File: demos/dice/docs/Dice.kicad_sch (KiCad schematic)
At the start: 23 parts, among them U2 CD4017

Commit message: export: kicad_sch — Phase 2.5b: layered placement, wire routing, KiCad 10 compatibility (#23)
* export: kicad_sch — Phase 2.5b: layered placement + routing + KiCad 9 fix

Placement (placement.py, complete rewrite):
- Replaces naive grid with Layered Signal Flow algorithm (spec §5 stages 1–8)
- Stage 1: band classification — power chips/rails at top, LEDs at bottom,
  everything else in the signal band
- Stage 2: signal-flow DAG via BFS from Rail/Connector sources; layer = BFS
  distance from nearest source
- Stage 3–4: place within (band, layer) cells at 1500-mil (38.1 mm) same-band
  spacing, 1000-mil inter-band gutter, 25.4 mm page margin
- Stage 6: cluster breakup — up to 10 iterations shifting same-band parts
  that land closer than 0.9× SAME_BAND_SPACING_MM
- Stage 8: page sized to fit (A4 → A3 → A2 → A1)
- grid_place() and sheet_size_mm() kept as shims for backward-compat

Routing (routing.py, new file):
- route_net(): connects stub ends with Manhattan L-shapes (horizontal first)
- find_junctions(): returns points where ≥3 wire endpoints coincide
- renderer uses routed wires between signal-net stub ends

Hierarchical (hierarchical.py, new file):
- collect_boards(), is_multi_board(), sub_sheet_filename() — interface stub
  for multi-Board sub-sheet emission (full implementation deferred)

KiCad 9 sub-symbol name fix (library_loader.py):
- KiCad 9 schematics expect sub-symbols nested inside their parent in
  lib_symbols to use the bare name (R_0_1, LED_0_1, 4069_1_0) — NOT the
  lib-qualified name (Device:R_0_1, Device:LED_0_1, 4xxx:4069_1_0)
- Fixed _qualify_names() to add the lib: prefix only to the exact parent
  symbol name using a lookahead (?=") that prevents sub-unit names from
  being qualified

Tests (+25 tests):
- test_placement.py: band classification, all-on-grid, determinism,
  minimum spacing, power < signal < indicator Y ordering, page sizing
- test_routing.py: H/V segments, L-shapes, orthogonality, grid snap,
  junction detection

Golden files re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
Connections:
- net Net-(D10-anode) is gone; now on net Net-(D1-cathode): D10.1 (K), D11.1 (K), R3.1, R3.2
- net Net-(D12-anode) is gone; now on net Net-(D1-cathode): D12.1 (K), D13.1 (K), R4.1, R4.2
- net Net-(D8-anode) is gone; now on net Net-(D1-cathode): D8.1 (K), D9.1 (K), R2.1, R2.2
- net Net-(D1-cathode): now also R5.1, R5.2, R6.1, R6.2, R7.1, R7.2
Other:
- moved on the sheet: C1, C2, D1, D10, D11, D12, D13, D2, D3, D4, D5, D6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

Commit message: framework: passive + diode terminals mandatory (#30)
Continuation of the LED.cathode regression fix (#29). Resistor,
Capacitor, Inductor, and every Diode subclass had their terminals
declared `mandatory=False` with the same "structurally inert under
graph evaluation" justification — letting demos declare BOM-only
timing / decoupling / pull-up parts without wiring them, then ship
breadboard SVGs and netlists where those parts sat orphaned.

A real resistor / capacitor / inductor / diode with a dangling
terminal does nothing. Marking the ports mandatory closes the
silent regression at the framework layer.

  - `src/components/passives/{resistor,capacitor,inductor}.py` and
    every diode subclass under `src/components/diodes/` now declare
    their terminals `mandatory=True`.
  - `tests/components/test_{resistor,capacitor,inductor}.py`:
    regression tests pin the new contract per component.
  - `tests/components/test_diode_mandatory_terminals.py` (new):
    parametrized over D1N4001 / D1N4007 / D1N4148 / D1N4728A /
    D1N4733A / D1N4742A / D1N5817.
  - Six demos (`backup_power`, `bldc_motor`, `dice`,
    `doorbell_protector`, `fan_cooling`, `isolated_rs232`) had
    declared-but-unwired passives — each now wires them either to
    their datasheet-correct net (e.g. DoorbellProtector's flyback
    diode anode joins the relay coil_minus net) or as an isolated
    0-Ω passthrough with `dynamically_driven=True` where the part
    is genuinely BOM-only and the voltage-only simulator can't
    honour its behaviour. Comments at each call site explain
    which kind.
  - Test fixtures across CLI, refdes, format-roundtrip, kicad
    import, and per-format renderer tests updated so they still
    pin down the specific error each one exists to catch without
    tripping the new mandatory-pin check first.
  - All demo docs regenerated; goldens refreshed.

After this commit the breadboard SVGs show every BOM part connected
to something — no more orphaned caps and resistors float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
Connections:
- net Net-(D1-cathode) is gone; now on net VCC: D10.1 (K), D11.1 (K), D12.1 (K), D13.1 (K), D7.1 (K), D8.1 (K), D9.1 (K), R1.1, R1.2, R2.1, R2.2, R3.1, R3.2, R4.1, R4.2, R5.1, R5.2, R6.1, R6.2, R7.1, R7.2
- net VCC: now reaches C2.1
- net VCC: now also C1.1, C1.2, C2.2
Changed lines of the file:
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@@
     (stroke (width 0) (type default))
+  )
+  (symbol
+    (lib_id "power:VCC")
+    (at 63.5 641.35 90)
+    (unit 1)
+    (exclude_from_sim no)
+    (in_bom yes)
+    (on_board yes)
+    (dnp no)
+    (property "Reference" "#PWR"
+      (at 63.5 641.35 0)
+      (effects (font (size 1.27 1.27)) (hide yes))
+    )
+    (property "Value" "VCC"
+      (at 63.5 641.35 0)
+      (effects (font (size 1.27 1.27)))
+    )
+    (pin "1")
   )
   (wire
     (pts (xy 63.5 631.19) (xy 63.5 628.65))
     (stroke (width 0) (type default))
+  )
+  (symbol
+    (lib_id "power:VCC")
+    (at 63.5 628.65 90)
+    (unit 1)
+    (exclude_from_sim no)
+    (in_bom yes)
+    (on_board yes)
+    (dnp no)
+    (property "Reference" "#PWR"
+      (at 63.5 628.65 0)
+      (effects (font (size 1.27 1.27)) (hide yes))
+    )
+    (property "Value" "VCC"
+      (at 63.5 628.65 0)
+      (effects (font (size 1.27 1.27)))
+    )
+    (pin "1")
   )
   (symbol
@@
     (stroke (width 0) (type default))
   )
+  (symbol
+    (lib_id "power:VCC")
+    (at 63.5 679.45 90)
+    (unit 1)
+    (exclude_from_sim no)
+    (in_bom yes)
+    (on_board yes)
+    (dnp no)
+    (property "Reference" "#PWR"
+      (at 63.5 679.45 0)
+      (effects (font (size 1.27 1.27)) (hide yes))
+    )
+    (property "Value" "VCC"
+      (at 63.5 679.45 0)
+      (effects (font (size 1.27 1.27)))
+    )
+    (pin "1")
+  )
   (wire
     (pts (xy 63.5 669.29) (xy 63.5 666.75))
     (stroke (width 0) (type default))
+  )
+  (symbol
+    (lib_id "power:VCC")
+    (at 63.5 666.75 90)
+    (unit 1)
+    (exclude_from_sim no)
+    (in_bom yes)
+    (on_board yes)
+    (dnp no)
+    (property "Reference" "#PWR"
+      (at 63.5 666.75 0)
+      (effects (font (size 1.27 1.27)) (hide yes))
+    )
+    (property "Value" "VCC"
+      (at 63.5 666.75 0)
+      (effects (font (size 1.27 1.27)))
+    )
+    (pin "1")
   )
   (symbol
@@
     (stroke (width 0) (type default))
   )
+  (symbol
+    (lib_id "power:VCC")
+    (at 63.5 717.55 90)
+    (unit 1)
+    (exclude_from_sim no)
+    (in_bom yes)
+    (on_board yes)
+    (dnp no)
+    (property "Reference" "#PWR"
+      (at 63.5 717.55 0)
+      (effects (font (size 1.27 1.27)) (hide yes))
+    )
+    (property "Value" "VCC"
+      (at 63.5 717.55 0)
+      (effects (font (size 1.27 1.27)))
+    )
+    (pin "1")
+  )
   (wire
     (pts (xy 63.5 707.39) (xy 63.5 704.85))
     (stroke (width 0) (type default))
+  )
+  (symbol
+    (lib_id "power:VCC")
+    (at 63.5 704.85 90)
+    (unit 1)
+    (exclude_from_sim no)
+    (in_bom yes)
+    (on_board yes)
+    (dnp no)
+    (property "Reference" "#PWR"
+      (at 63.5 704.85 0)
+      (effects (font (size 1.27 1.27)) (hide yes))
+    )
+    (property "Value" "VCC"
+      (at 63.5 704.85 0)
+      (effects (font (size 1.27 1.27)))
+    )
+    (pin "1")
   )
   (symbol
@@
     (stroke (width 0) (type default))
   )
+  (symbol
+    (lib_id "power:VCC")
+    (at 63.5 31.75 90)
+    (unit 1)
+    (exclude_from_sim no)
+    (in_bom yes)
+    (on_board yes)
+    (dnp no)
+    (property "Reference" "#PWR"
+      (at 63.5 31.75 0)
+      (effects (font (size 1.27 1.27)) (hide yes))
+    )
+    (property "Value" "VCC"
+      (at 63.5 31.75 0)
+      (effects (font (size 1.27 1.27)))
+    )
+    (pin "1")
+  )
   (wire
     (pts (xy 63.5 21.59) (xy 63.5 19.05))
     (stroke (width 0) (type default))
+  )
+  (symbol
+    (lib_id "power:VCC")
+    (at 63.5 19.05 90)
+    (unit 1)
+    (exclude_from_sim no)
+    (in_bom yes)
+    (on_board yes)
+    (dnp no)
+    (property "Reference" "#PWR"
+      (at 63.5 19.05 0)
+      (effects (font (size 1.27 1.27)) (hide yes))
+    )
+    (property "Value" "VCC"
+      (at 63.5 19.05 0)
+      (effects (font (size 1.27 1.27)))
+    )
+    (pin "1")
   )
   (symbol
@@
     (stroke (width 0) (type default))
   )
+  (symbol
+    (lib_id "power:VCC")
+    (at 63.5 69.85 90)
+    (unit 1)
+    (exclude_from_sim no)
+    (in_bom yes)
+    (on_board yes)
+    (dnp no)
+    (property "Reference" "#PWR"
+      (at 63.5 69.85 0)
+      (effects (font (size 1.27 1.27)) (hide yes))
+    )
+    (property "Value" "VCC"
+      (at 63.5 69.85 0)
+      (effects (font (size 1.27 1.27)))
+    )
+    (pin "1")
+  )
   (wire
     (pts (xy 63.5 59.69) (xy 63.5 57.15))
@@
   )
   (symbol
+    (lib_id "power:VCC")
+    (at 63.5 57.15 90)
+    (unit 1)
+    (exclude_from_sim no)
+    (in_bom yes)
+    (on_board yes)
+    (dnp no)
+    (property "Reference" "#PWR"
+      (at 63.5 57.15 0)
+      (effects (font (size 1.27 1.27)) (hide yes))
+    )
+    (property "Value" "VCC"
+      (at 63.5 57.15 0)
+      (effects (font (size 1.27 1.27)))
+    )
+    (pin "1")
+  )
+  (symbol

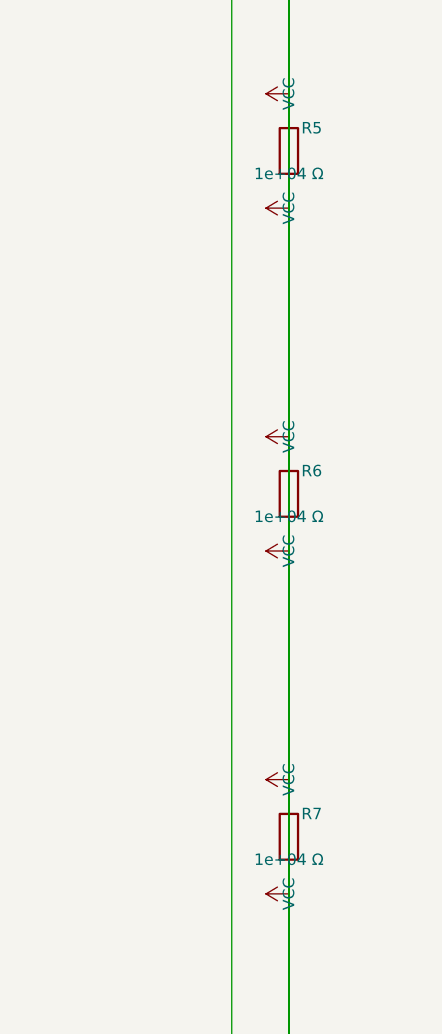
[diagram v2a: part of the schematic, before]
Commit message: units: Ohms.__str__ uses engineering notation (kΩ, MΩ, GΩ)
The previous `Ohms.__str__` formatted with bare `:.3g`, producing
unreadable scientific output for clean kilo / mega multiples:

  str(Ohms(10_000))     == "1e+04 Ω"      → now "10 kΩ"
  str(Ohms(100_000))    == "1e+05 Ω"      → now "100 kΩ"
  str(Ohms(1_000_000))  == "1e+06 Ω"      → now "1 MΩ"

The breadboard SVG visualiser surfaced the problem: a resistor body
labelled "100000Ω" makes a reader count zeros, while a label of
"100 kΩ" reads at a glance — exactly the convention every schematic
and parts catalogue uses. Centralising the engineering notation in
`Ohms.__str__` means every downstream consumer (assembly guide,
breadboard SVG, kicad netlist, BOM, reports) inherits the readable
form without each format adapter rolling its own formatter.

  - `Ohms.__str__` returns "47 Ω", "4.7 kΩ", "10 kΩ", "100 kΩ",
    "1 MΩ", "10 MΩ", "1 GΩ" per the kilo / mega / giga thresholds.
  - `Resistor.__str__` delegates to `str(self._ohms)` so it
    inherits the new notation (was producing the noisy "47.0 Ω"
    via raw float).
  - The breadboard visualiser's resistor body label uses
    `str(part.ohms)` directly (previously had a private
    `_format_ohms_compact` helper; removed).
  - `tests/components/test_resistor.py::test_str` updated for
    "47 Ω" (was "47.0 Ω"); new `test_str_renders_in_engineering_notation`
    pins kΩ / MΩ output across the kilo and mega thresholds.
  - All demo docs / goldens refreshed where the Ohms.__str__
    change affected the rendered output (breadboard SVGs, kicad
    sch value fields, BOM rows).
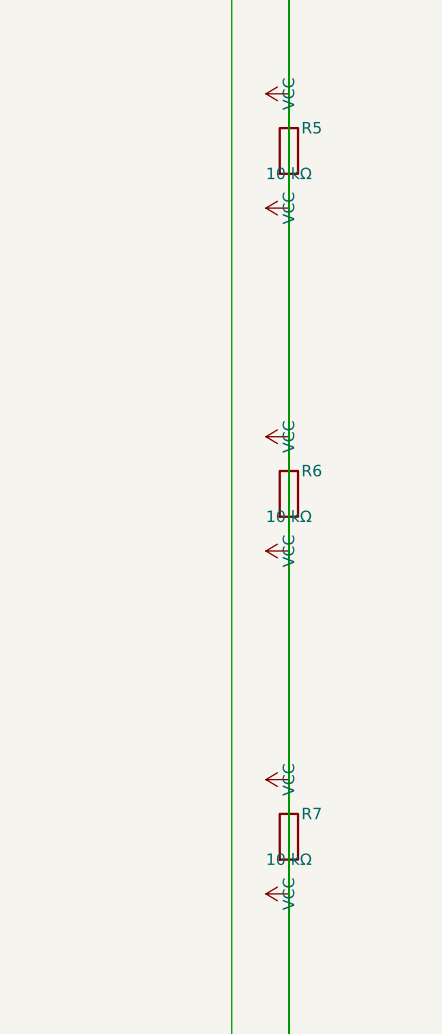
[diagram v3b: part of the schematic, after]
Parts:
- R5, R6, R7: value 1e+04 Ω -> 10 kΩ
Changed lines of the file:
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@@
       (effects (font (size 1.27 1.27)))
     )
-    (property "Value" "1e+04 Ω"
+    (property "Value" "10 kΩ"
       (at 63.5 637.54 0)
       (effects (font (size 1.27 1.27)))
@@
       (effects (font (size 1.27 1.27)))
     )
-    (property "Value" "1e+04 Ω"
+    (property "Value" "10 kΩ"
       (at 63.5 675.64 0)
       (effects (font (size 1.27 1.27)))
@@
       (effects (font (size 1.27 1.27)))
     )
-    (property "Value" "1e+04 Ω"
+    (property "Value" "10 kΩ"
       (at 63.5 713.74 0)
       (effects (font (size 1.27 1.27)))

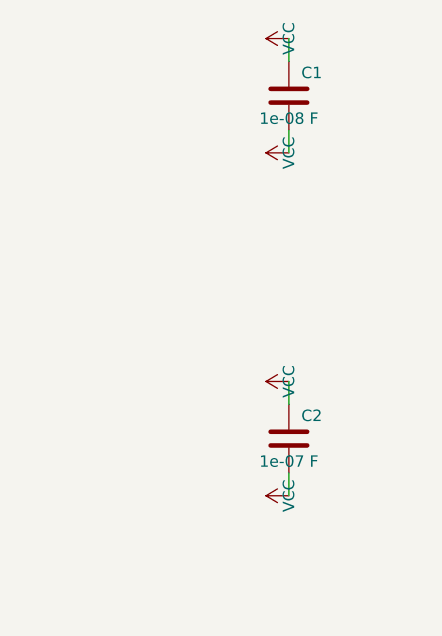
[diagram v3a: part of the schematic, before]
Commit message: units: Farads + Henries __str__ also use engineering notation
Same treatment as `Ohms.__str__` (previous commit) for the other two
passive engineering quantities. Demos contain caps and inductors
with values that the bare `:.3g` formatter would emit in scientific
form (`1e-07 F` for a 100 nF decoupling cap); centralising the
engineering notation on the unit class means every consumer
(reports, BOM, breadboard SVG, etc.) inherits the readable form.

  - `Farads.__str__` returns `100 pF`, `22 nF`, `100 nF`, `1 µF`,
    `4.7 µF`, `470 µF`, `1 mF`, `1 F` across the standard
    capacitance bands.
  - `Henries.__str__` returns `100 nH`, `10 µH`, `22 mH`, `1 H`
    across the standard inductance bands.
  - `Capacitor.__str__` and `Inductor.__str__` delegate to the
    unit class's str (were rolling raw-float formatters).
  - `framework.export.reports_common.part_description` now uses
    `str(part.ohms / farads / henries)` directly instead of the
    parallel `_format_ohms` / `_format_farads` / `_format_henries`
    helpers (removed — they duplicated the new logic on raw
    floats).
  - Breadboard SVG renderer now also labels capacitor and inductor
    bodies with their engineering-notation value (was only
    resistors).
  - `tests/framework/test_units.py`: parametrised regression tests
    for both unit classes across every band.
  - All affected demo docs / goldens refreshed.
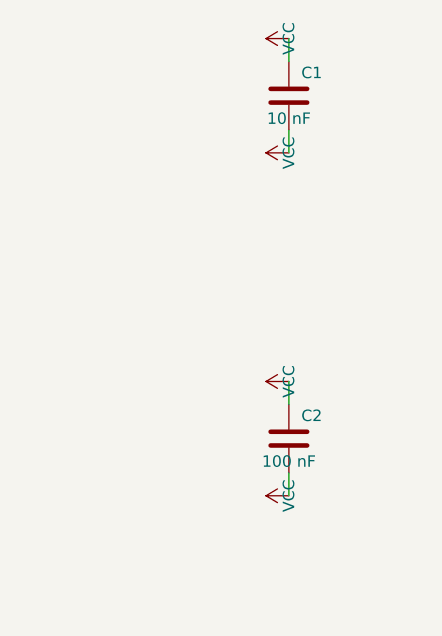
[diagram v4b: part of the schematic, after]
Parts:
- C1: value 1e-08 F -> 10 nF
- C2: value 1e-07 F -> 100 nF
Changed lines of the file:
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@@
       (effects (font (size 1.27 1.27)))
     )
-    (property "Value" "1e-08 F"
+    (property "Value" "10 nF"
       (at 63.5 27.94 0)
       (effects (font (size 1.27 1.27)))
@@
       (effects (font (size 1.27 1.27)))
     )
-    (property "Value" "1e-07 F"
+    (property "Value" "100 nF"
       (at 63.5 66.04 0)
       (effects (font (size 1.27 1.27)))
